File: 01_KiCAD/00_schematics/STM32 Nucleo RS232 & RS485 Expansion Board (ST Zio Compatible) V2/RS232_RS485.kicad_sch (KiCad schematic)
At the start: 0 parts

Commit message: Add THVD4431 & Phoenic 4-p connector
Added the THVD4431 dual Tranceiver Chip and modified schematic symbol.
Added the RS485 Phoenix Contact connector (pn 1190299)
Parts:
- added J1: 1190299, PH1190299:PHOENIX_1190299, symbol PH1190299:1190299
- added U1: THVD4431RHAR, THVD4431RHAR:RHA0040R-MFG, symbol THVD4431RHAR:THVD4431RHAR

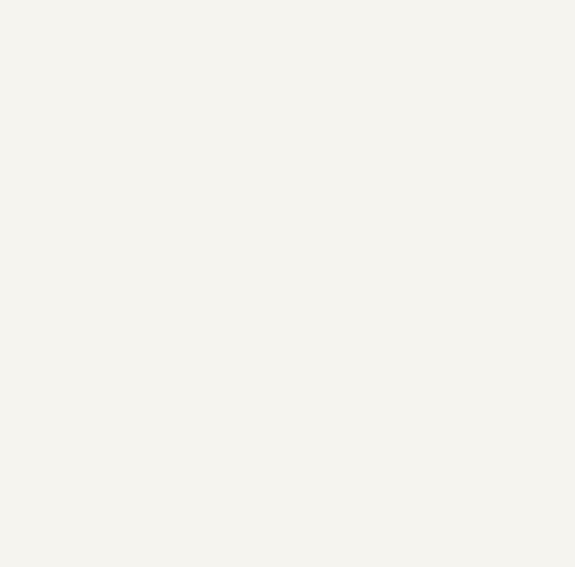
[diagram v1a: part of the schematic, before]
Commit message: Added SubD 9-P connector
Added the RS232 SubD connector
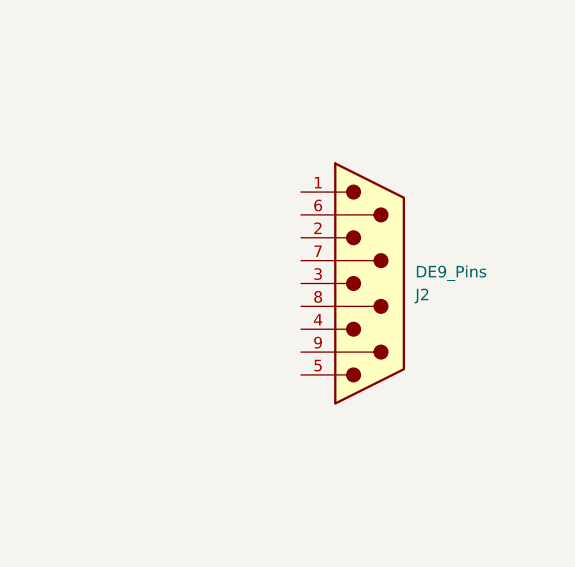
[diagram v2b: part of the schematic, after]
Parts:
- added J2: DE9_Pins, symbol Connector:DE9_Pins
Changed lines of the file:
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@@
+		)
+	)
+	(symbol
+		(lib_id "Connector:DE9_Pins")
+		(at 264.16 92.71 0)
+		(mirror x)
+		(unit 1)
+		(exclude_from_sim no)
+		(in_bom yes)
+		(on_board yes)
+		(dnp no)
+		(property "Reference" "J2"
+			(at 269.24 93.9801 0)
+			(effects
+				(font
+					(size 1.27 1.27)
+				)
+				(justify left)
+			)
+		)
+		(property "Value" "DE9_Pins"
+			(at 269.24 91.4401 0)
+			(effects
+				(font
+					(size 1.27 1.27)
+				)
+				(justify left)
+			)
+		)
+		(property "Footprint" ""
+			(at 264.16 92.71 0)
+			(effects
+				(font
+					(size 1.27 1.27)
+				)
+				(hide yes)
+			)
+		)
+		(property "Datasheet" "~"
+			(at 264.16 92.71 0)
+			(effects
+				(font
+					(size 1.27 1.27)
+				)
+				(hide yes)
+			)
+		)
+		(property "Description" "9-pin D-SUB connector, pins (male)"
+			(at 264.16 92.71 0)
+			(effects
+				(font
+					(size 1.27 1.27)
+				)
+				(hide yes)
+			)
+		)
+		(pin "4"
+		)
+		(pin "2"
+		)
+		(pin "6"
+		)
+		(pin "1"
+		)
+		(pin "7"
+		)
+		(pin "8"
+		)
+		(pin "3"
+		)
+		(pin "5"
+		)
+		(pin "9"
+		)
+		(instances
+			(project ""
+				(path "/080f83b7-8913-48e8-ab8e-79cb12295542/eb278bca-04f9-4d71-99cd-ac1b982e4a86"
+					(reference "J2")
+					(unit 1)
+				)
+			)
 		)
 	)

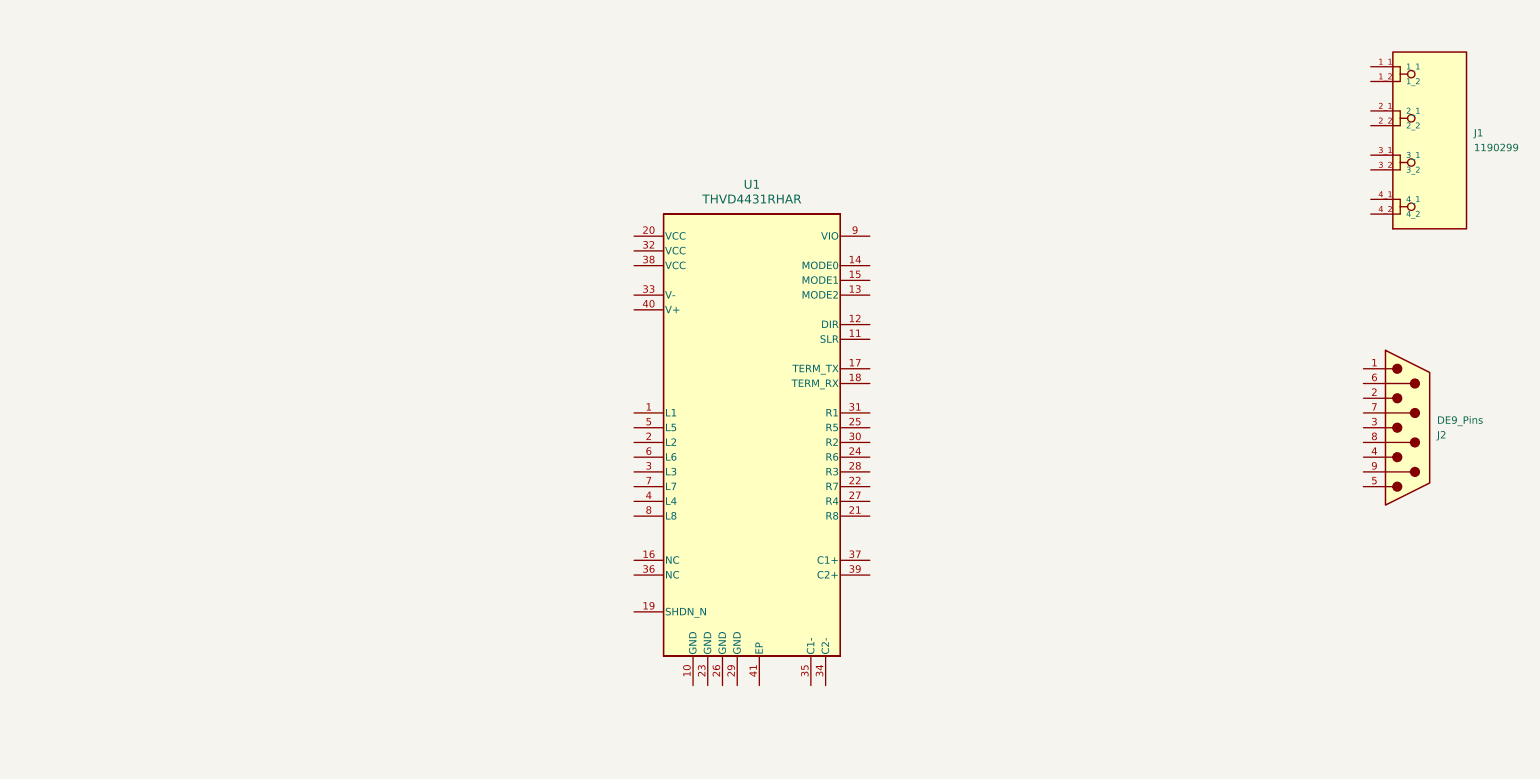
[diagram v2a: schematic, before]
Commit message: Added components
Added R1 - R4 0R pass-through resistors for RS485 data lines to seperate them from RS232 Net
Added capacitors C1+ and C2+ for charge pump
Completed table on root page for THVD4431 and ZIO Connector Pin Layout
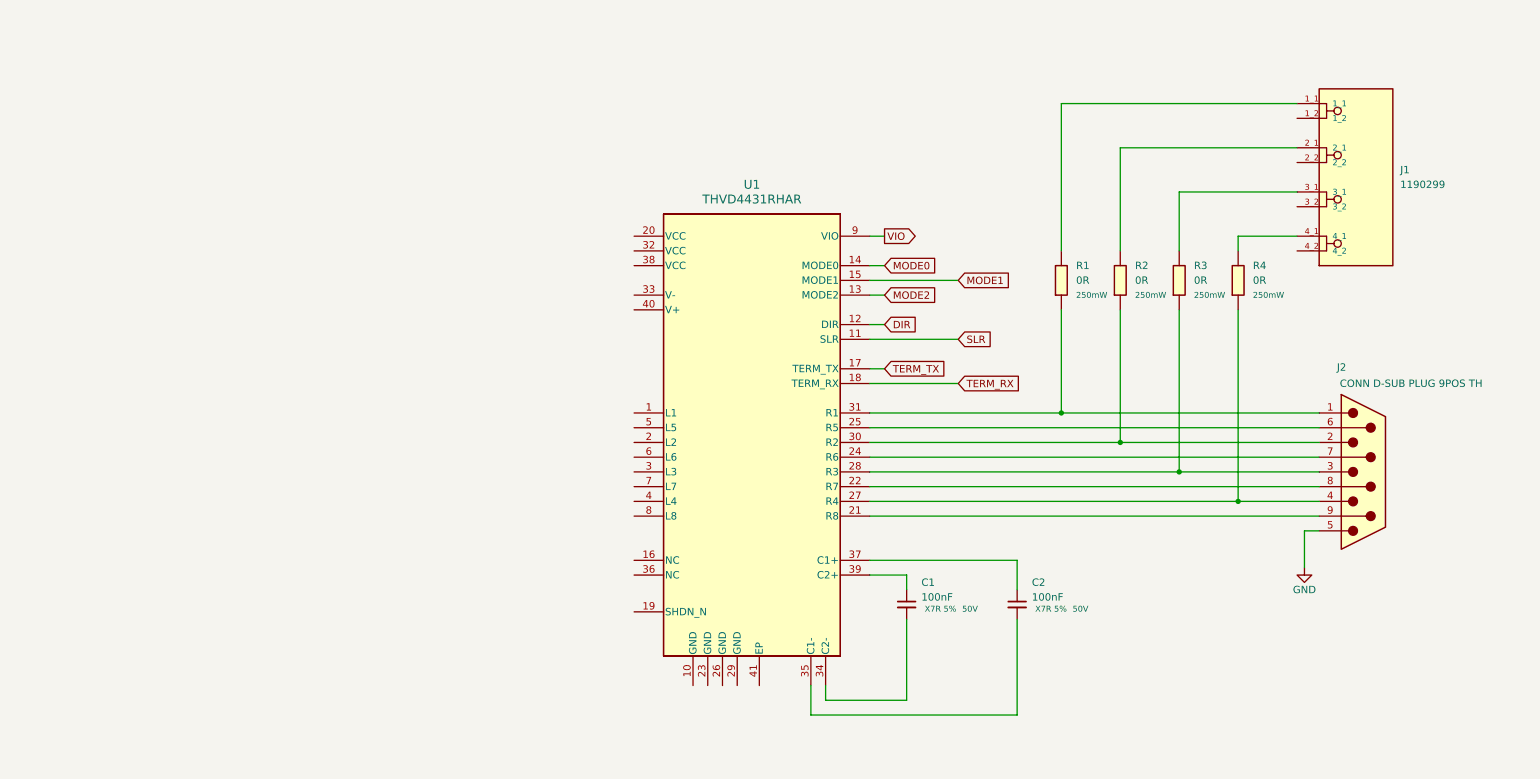
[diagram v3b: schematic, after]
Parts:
- added C1, C2: 100nF, PCM_SparkFun-Capacitor:C_0603_1608Metric, symbol PCM_SparkFun-Capacitor:0.1uF_0603_25V_20%
- added R1, R2, R3, R4: 0R, PCM_fab:R_0603, symbol PCM_fab:R_0603
- J1: LCSC (none) -> C3309834; MPN (none) -> 1190299; Manufacturer (none) -> Phoenix Contact; Type (none) -> THT
- J2: value DE9_Pins -> CONN D-SUB PLUG 9POS TH; LCSC (none) -> C591554; MPN (none) -> 2301843-2; Manufacturer (none) -> TE Connectivity; Package (none) -> Through Hole; Type (none) -> THT
- U1: LCSC (none) -> C22445427; MPN (none) -> THVD4431RHAR; Manufacturer (none) -> TI; Package (none) -> VQFN-40-EP(6x6); Type (none) -> SMD
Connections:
- net SLR: now reaches U1.11 (SLR)
- net DIR: now reaches U1.12 (DIR)
- net MODE2: now reaches U1.13 (MODE2)
- net MODE0: now reaches U1.14 (MODE0)
- net MODE1: now reaches U1.15 (MODE1)
- net TERM_TX: now reaches U1.17 (TERM_TX)
- net TERM_RX: now reaches U1.18 (TERM_RX)
- net at U1.21 (R8): now also J2.9
- net at U1.22 (R7): now also J2.8
- net at U1.24 (R6): now also J2.7
- net at U1.25 (R5): now also J2.6
- net at U1.27 (R4): now also J2.4, R4.2
- net at U1.28 (R3): now also J2.3, R3.2
- net at U1.30 (R2): now also J2.2, R2.2
- net at U1.31 (R1): now also J2.1, R1.2
- net at U1.34 (C2-): now also C1.2
- net at U1.35 (C1-): now also C2.2
- net at U1.37 (C1+): now also C2.1
- net at U1.39 (C2+): now also C1.1
- net VIO: now reaches U1.9 (VIO)
- net at J1.1_1: now also R1.1
- net at J1.2_1: now also R2.1
- net at J1.3_1: now also R3.1
- net at J1.4_1: now also R4.1
- net GND: now reaches J2.5
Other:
- moved on the sheet: J1, J2

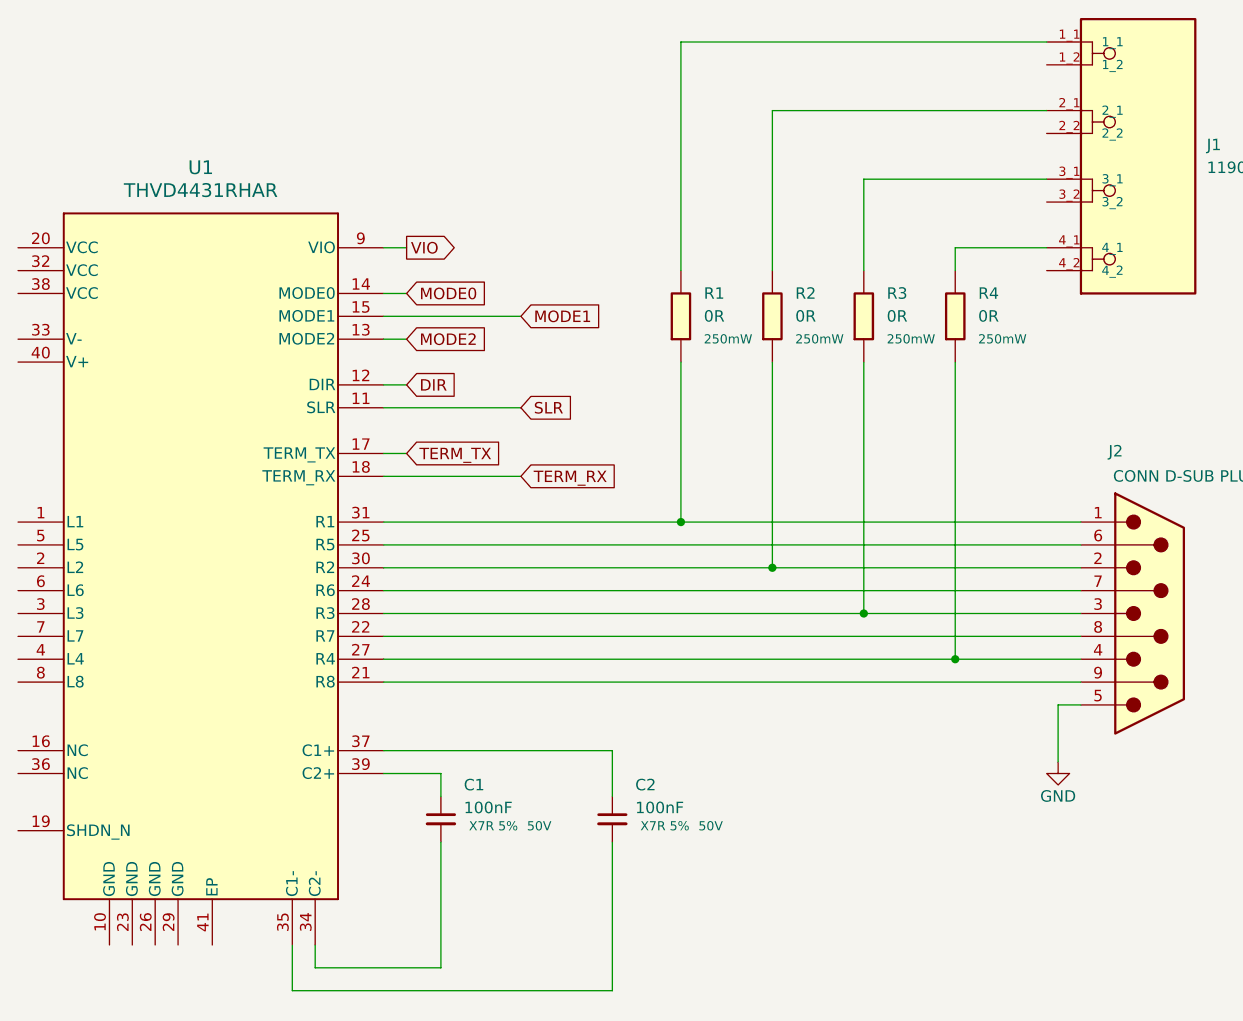
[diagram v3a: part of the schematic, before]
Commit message: Complemented descriptions
Complemented the RS232, RS485 and THVD4431 description table on the Root page
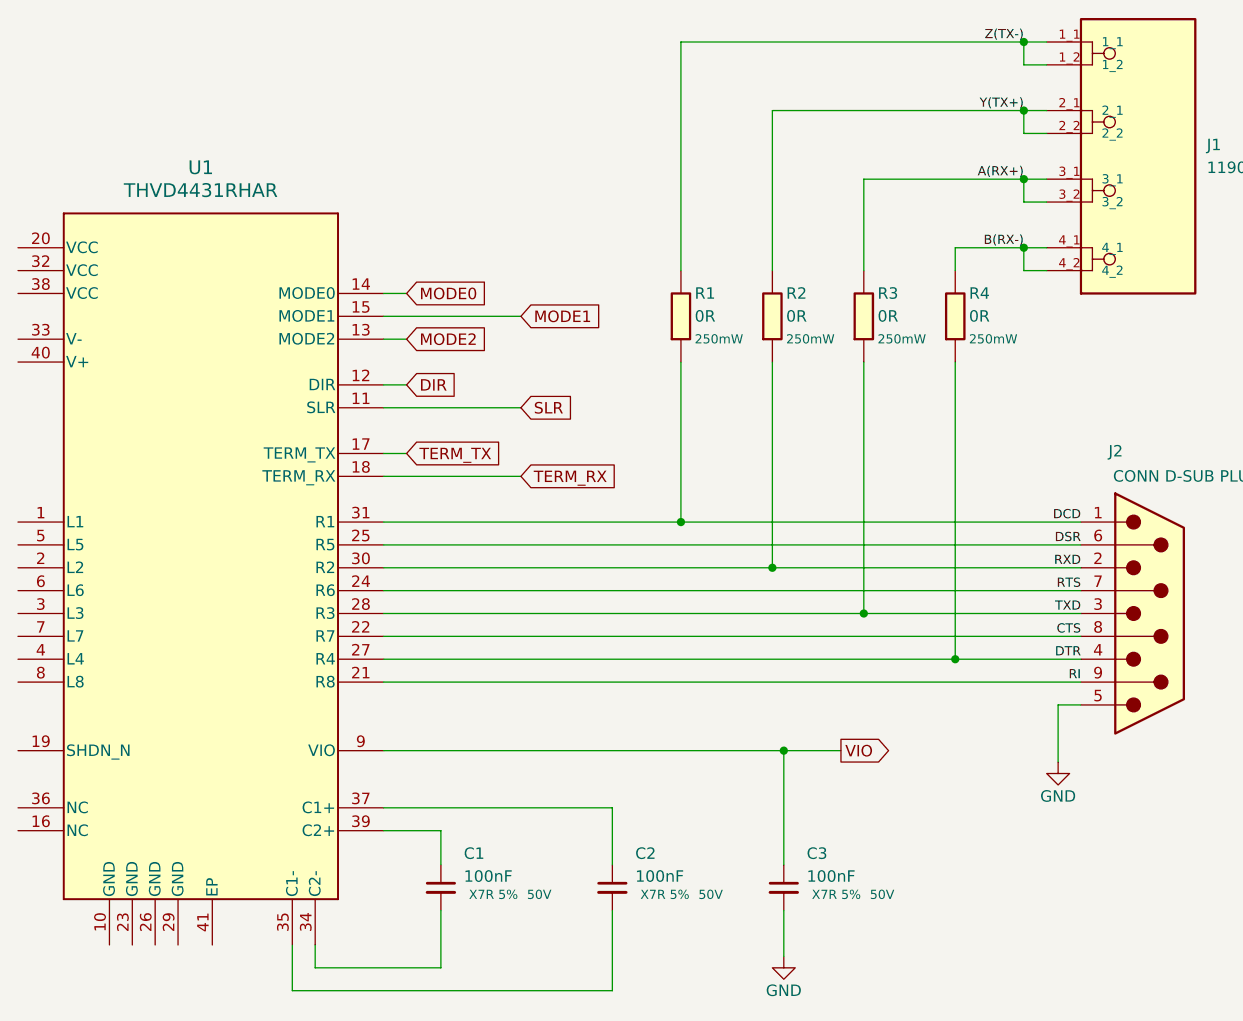
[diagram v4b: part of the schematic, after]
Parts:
- added C3: 100nF, PCM_SparkFun-Capacitor:C_0603_1608Metric, symbol PCM_SparkFun-Capacitor:0.1uF_0603_25V_20%
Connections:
- net GND: now also C3.2
- net VIO: now also C3.1
- net Y(TX+): now reaches J1.2_1, R2.1
- net Y(TX+): now also J1.2_2
- net RXD: now reaches J2.2, R2.2, U1.30 (R2)
- net RI: now reaches J2.9, U1.21 (R8)
- net CTS: now reaches J2.8, U1.22 (R7)
- net RTS: now reaches J2.7, U1.24 (R6)
- net DSR: now reaches J2.6, U1.25 (R5)
- net DTR: now reaches J2.4, R4.2, U1.27 (R4)
- net TXD: now reaches J2.3, R3.2, U1.28 (R3)
- net DCD: now reaches J2.1, R1.2, U1.31 (R1)
- net Z(TX-): now reaches J1.1_1, R1.1
- net Z(TX-): now also J1.1_2
- net A(RX+): now reaches J1.3_1, R3.1
- net A(RX+): now also J1.3_2
- net B(RX-): now reaches J1.4_1, R4.1
- net B(RX-): now also J1.4_2
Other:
- moved on the sheet: C1, C2

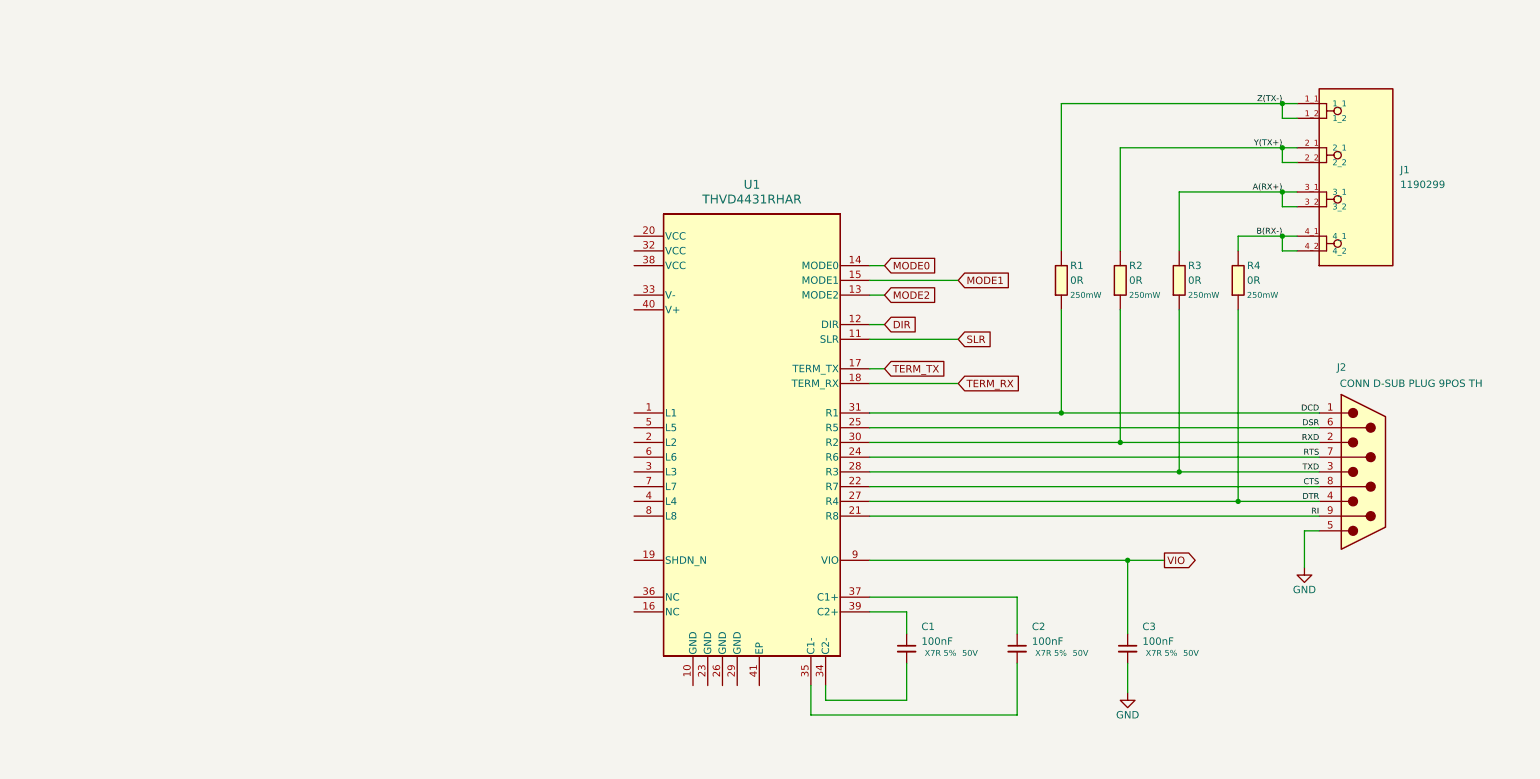
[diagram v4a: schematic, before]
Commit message: Added SHDN logic
Added the SHDN pin logic to have both hardware control and software control vor activating the THVD4431
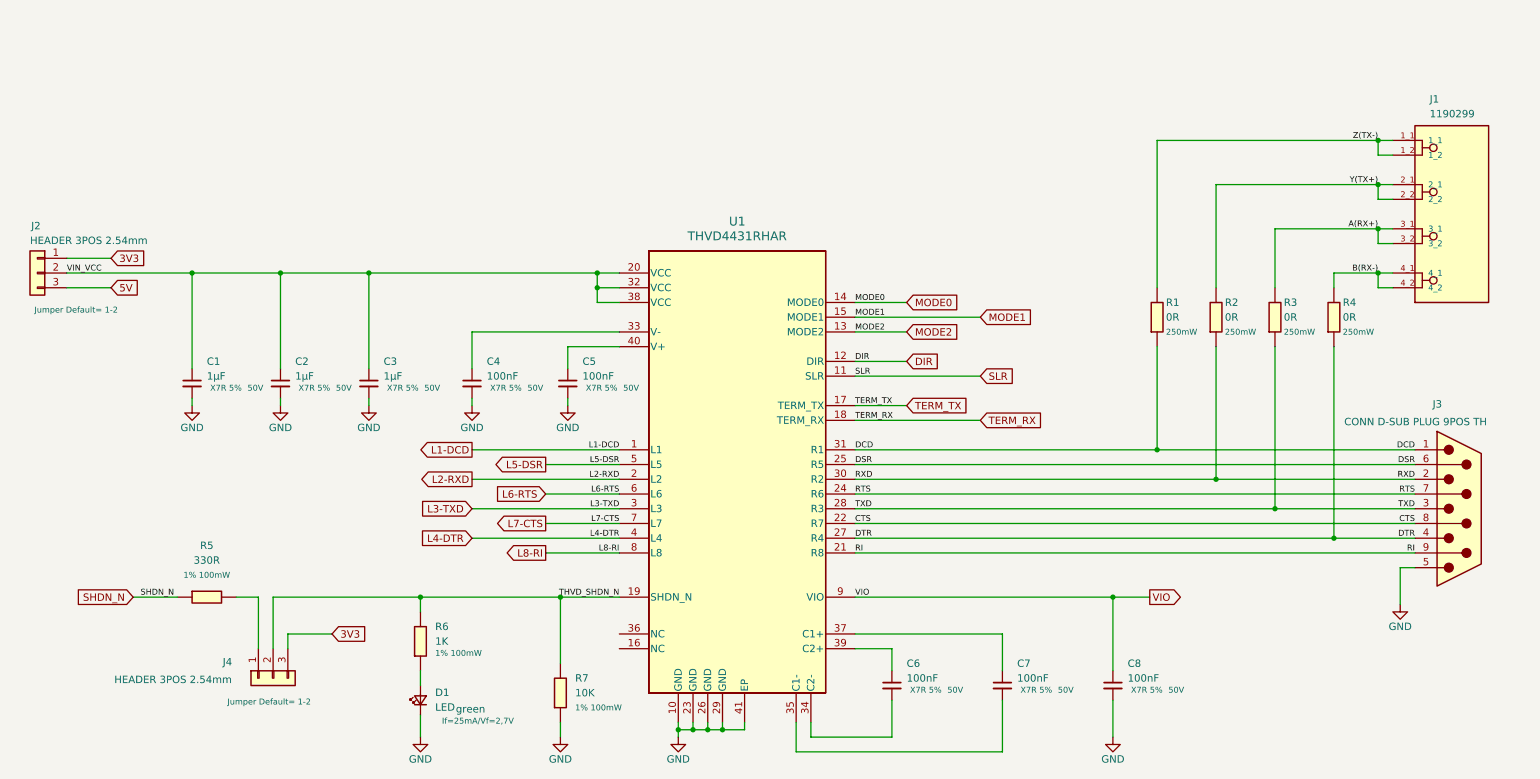
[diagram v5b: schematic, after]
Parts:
- added C1, C2, C3: 1µF, PCM_SparkFun-Capacitor:C_0603_1608Metric, symbol PCM_SparkFun-Capacitor:0.1uF_0603_25V_20%
- added C4, C5: 100nF, PCM_SparkFun-Capacitor:C_0603_1608Metric, symbol PCM_SparkFun-Capacitor:0.1uF_0603_25V_20%
- added D1: LED, IN-S63AT:LED_0603_WRE, symbol PCM_SparkFun-LED:LED
- added J2, J4: HEADER 3POS 2.54mm, symbol Connector_Generic:Conn_01x03
- added R5: 330R, PCM_fab:R_0603, symbol PCM_fab:R_0603
- added R6: 1K, PCM_fab:R_0603, symbol PCM_fab:R_0603
- added R7: 10K, PCM_fab:R_0603, symbol PCM_fab:R_0603
- renumbered C1 to C6, C2 to C7, C3 to C8, J2 to J3
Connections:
- net GND: now also U1.10 (GND), U1.23 (GND), U1.26 (GND), U1.29 (GND), U1.41 (EP), C1.2, C2.2, C3.2, C4.2, C5.2, D1.1 (K), R7.2
- net L1-DCD: now reaches U1.1 (L1)
- net THVD_SHDN_N: now reaches U1.19 (SHDN_N)
- net THVD_SHDN_N: now also J4.2 (Pin_2), R6.1, R7.1
- net L2-RXD: now reaches U1.2 (L2)
- net VIN_VCC: now reaches U1.20 (VCC)
- net VIN_VCC: now also U1.32 (VCC), U1.38 (VCC), C1.1, C2.1, C3.1, J2.2 (Pin_2)
- net L3-TXD: now reaches U1.3 (L3)
- net at U1.33 (V-): now also C4.1
- net L4-DTR: now reaches U1.4 (L4)
- net at U1.40 (V+): now also C5.1
- net L5-DSR: now reaches U1.5 (L5)
- net L6-RTS: now reaches U1.6 (L6)
- net L7-CTS: now reaches U1.7 (L7)
- net L8-RI: now reaches U1.8 (L8)
- new net: J4.1 (Pin_1), R5.1
- new net: D1.2 (A), R6.2
- new net 3V3: J2.1 (Pin_1), J4.3 (Pin_3)
- new net 5V: J2.3 (Pin_3)
- new net SHDN_N: R5.2
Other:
- moved on the sheet: C6, C7, C8, J1, J3, R1, R2, R3, R4, U1
